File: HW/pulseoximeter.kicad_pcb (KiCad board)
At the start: 4 copper layers, 42.5 x 82.4 mm, 49 parts, among them J1 X05A20L15T, J2 TYPE-C-31-M-12, U1 TPD2EUSB30DRTR, U2 TPS7A4700RGWR, U3 ESP32-S3-MINI-1-N8, U4 LM324, U6 OPA140AIDBVR

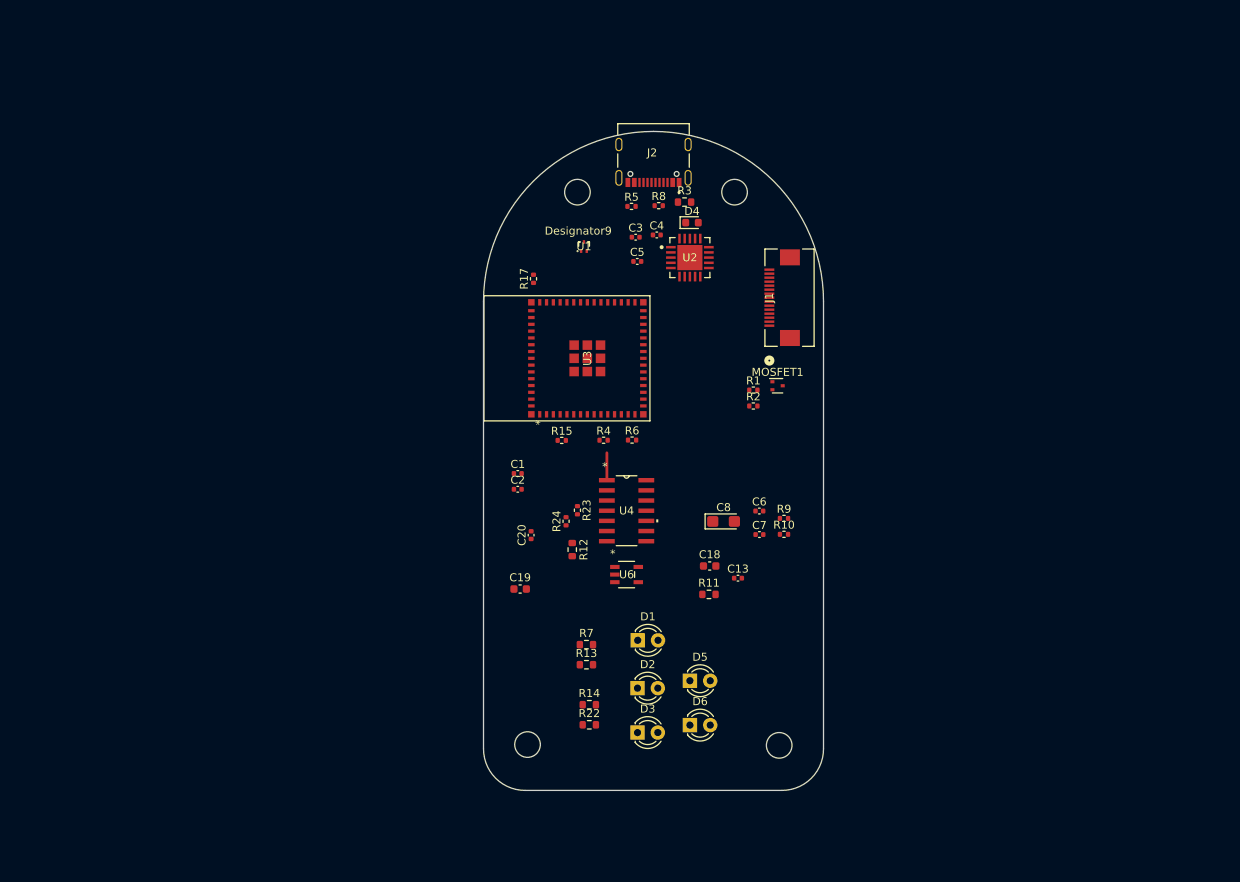
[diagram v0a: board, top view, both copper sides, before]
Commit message: implemented dynamic chart y-axis scaling
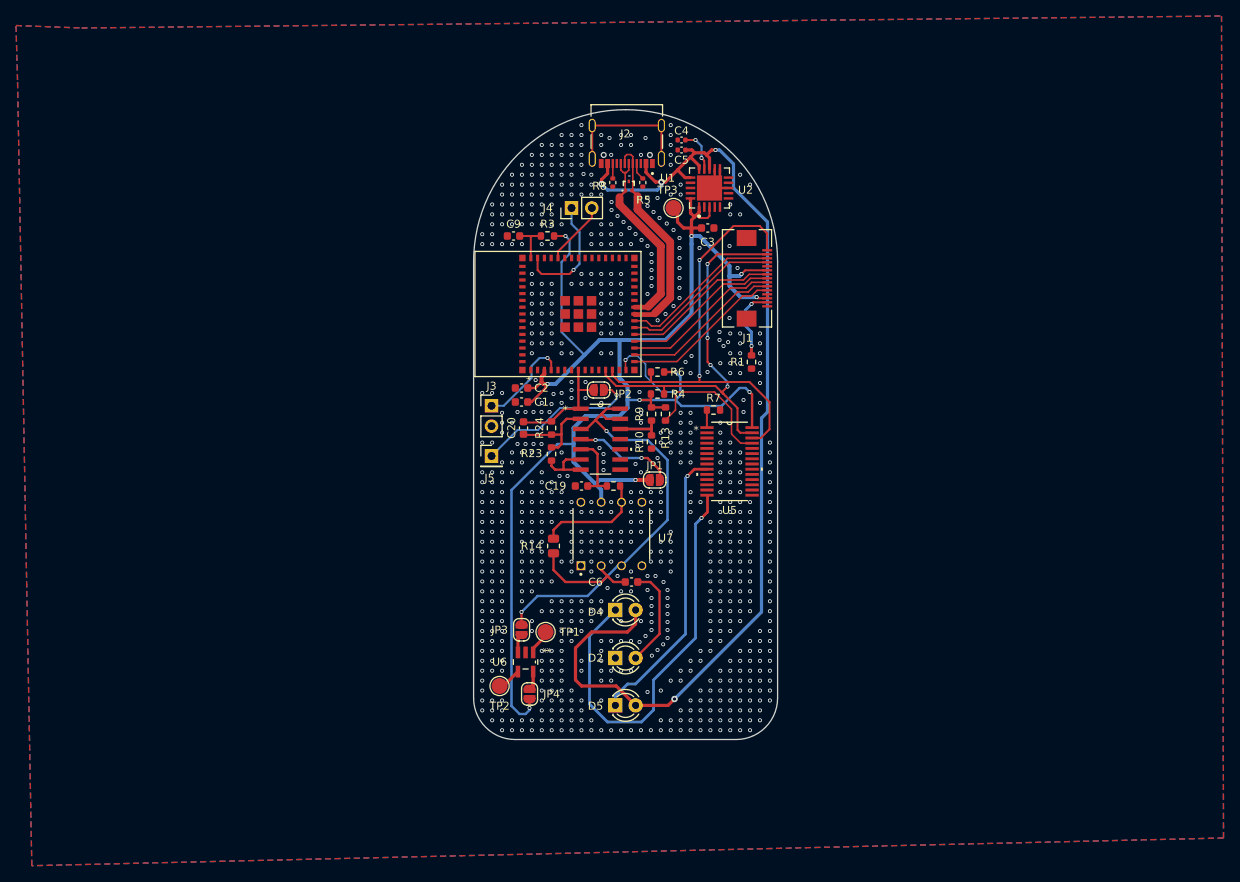
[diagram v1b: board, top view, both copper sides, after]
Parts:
- removed C13, C7: 0.1uF, Capacitor_SMD:C_0402_1005Metric
- removed C18: 440pF, Capacitor_SMD:C_0603_1608Metric
- removed C8: 1uF, Capacitor_Tantalum_SMD:CP_EIA-3216-10_Kemet-I
- removed D1: D_Photo, LED_THT:LED_D3.0mm
- removed D3, D6: LED, LED_THT:LED_D3.0mm
- removed MOSFET1: DMN2310UT-13, Package_TO_SOT_SMD:SOT-523
- removed R11: 8.1M, Resistor_SMD:R_0603_1608Metric
- removed R15, R17: 10k, Resistor_SMD:R_0402_1005Metric
- removed R2: 1M, Resistor_SMD:R_0402_1005Metric
- removed R22: 330, Resistor_SMD:R_0603_1608Metric
- removed REF** (x4): MountingHole_3.2mm_M3, MountingHole:MountingHole_3.2mm_M3
- added C9: 0.1uF, Capacitor_SMD:C_0603_1608Metric, F.Cu at (131.5, 68.5)
- added J3: Conn_01x02, Connector_PinHeader_2.54mm:PinHeader_1x02_P2.54mm_Vertical, F.Cu at (128.8, 89.7)
- added J4: Conn_01x02, Connector_PinHeader_2.54mm:PinHeader_1x02_P2.54mm_Vertical, F.Cu at (138.8, 65.0)
- added J5: Conn_01x01_Socket, Connector_PinHeader_2.54mm:PinHeader_1x01_P2.54mm_Vertical, F.Cu at (128.8, 96.0)
- added JP1: SolderJumper_2_Open, Jumper:SolderJumper-2_P1.3mm_Open_RoundedPad1.0x1.5mm, F.Cu at (149.2, 99.0)
- added JP2: SolderJumper_2_Open, Jumper:SolderJumper-2_P1.3mm_Open_RoundedPad1.0x1.5mm, F.Cu at (142.2, 87.8)
- added JP3: SolderJumper_2_Open, Jumper:SolderJumper-2_P1.3mm_Open_RoundedPad1.0x1.5mm, F.Cu at (132.5, 117.7)
- added JP4: SolderJumper_2_Open, Jumper:SolderJumper-2_P1.3mm_Open_RoundedPad1.0x1.5mm, F.Cu at (133.5, 125.8)
- added TP1: TestPoint, TestPoint:TestPoint_Pad_D2.0mm, F.Cu at (135.5, 118.0)
- added TP2: TestPoint, TestPoint:TestPoint_Pad_D2.0mm, F.Cu at (129.8, 124.8)
- added TP3: TestPoint, TestPoint:TestPoint_Pad_D2.0mm, F.Cu at (151.5, 65.0)
- added U5: TLC59116IPWR, TLC59116IPWR:PW28, F.Cu at (158.5, 96.7)
- added U7: LMC6001BIN/NOPB, LMC6001BIN_NOPB:DIP794W45P254L959H508Q8, F.Cu at (143.7, 105.8)
- C1, C2, C20, C3: footprint Capacitor_SMD:C_0402_1005Metric -> Capacitor_SMD:C_0603_1608Metric
- C6: value 10uF -> 0.22uF; footprint Capacitor_SMD:C_0402_1005Metric -> Capacitor_SMD:C_0603_1608Metric
- D2: value LED -> D_Photo
- D4: footprint LED_SMD:LED_0603_1608Metric -> LED_THT:LED_D3.0mm
- R1: value 10k -> 0; footprint Resistor_SMD:R_0402_1005Metric -> Resistor_SMD:R_0603_1608Metric
- R10, R23, R24, R4, R6, R9: footprint Resistor_SMD:R_0402_1005Metric -> Resistor_SMD:R_0603_1608Metric
- R12: value 33k -> 22k
- R13: value 330 -> 10k
- R14: value 330 -> 5.6M; footprint Resistor_SMD:R_0603_1608Metric -> Resistor_SMD:R_0805_2012Metric
- R3: value 1k -> 10k
- R7: value 330 -> 910
- U6: footprint OPA140AIDBVR:DBV5-M -> OPA140AIDBVR:DBV5
- moved D4 49.4 mm to (144.2, 115.2)
- moved R7 33.4 mm to (156.5, 90.2), turned to 180 degrees
- moved R13 32.9 mm to (150.5, 90.8), turned to 90 degrees
- moved R9 21.1 mm to (148.8, 90.8), turned to -90 degrees
- moved R14 20.3 mm to (136.5, 107.2), turned to -90 degrees
- moved R10 20.2 mm to (148.8, 94.2), turned to -90 degrees
- moved C6 18.3 mm to (146.2, 111.8), turned to 180 degrees
- moved R3 17.6 mm to (135.8, 68.5), turned to 180 degrees
- moved U6 16.7 mm to (133.0, 121.8), turned to -90 degrees
- moved C19 15.0 mm to (140.0, 99.8), turned to 180 degrees
- moved C5 15.0 mm to (152.5, 57.8), turned to 180 degrees
- moved C20 13.4 mm to (132.8, 92.5), turned to -90 degrees
- moved C2 12.7 mm to (132.5, 87.5), turned to 180 degrees
- moved C4 12.3 mm to (152.5, 56.5)
- moved R24 11.8 mm to (136.3, 92.5), turned to -90 degrees
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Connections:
- C20 pad 2: Net-(U4A-+) -> Net-(U4A--)
- C6 pad 1: VBUS -> Net-(D2-A)
- C6 pad 2: GND -> Net-(U7-IN-)
- D4 pad 1: GND -> Net-(D4-K)
- D4 pad 2: Net-(D4-A) -> VBUS
- D5 pad 1: GND -> Net-(D5-K)
- D5 pad 2: Net-(D5-A) -> VBUS
- J1 pad 1: GND -> SCL
- J1 pad 10: +3.3V -> /DISPLAY_CS
- J1 pad 11: GND -> /DISPLAY_D/C
- J1 pad 12: /TP_RST -> +3.3V
- J1 pad 13: /TP_INT -> +3.3V
- J1 pad 14: SDA -> Net-(J1-Pad14)
- J1 pad 15: SCL -> GND
- J1 pad 2: /LEDK -> SDA
- J1 pad 3: +3.3V -> /TP_INT
- J1 pad 4: +3.3V -> /TP_RST
- J1 pad 5: /DISPLAY_D/C -> GND
- J1 pad 6: /DISPLAY_CS -> +3.3V
- J1 pad 7: /DISPLAY_CLK -> /DISPLAY_RESET
- J1 pad 9: /DISPLAY_RESET -> /DISPLAY_CLK
- R1 pad 1: Net-(MOSFET1-G) -> GND
- R1 pad 2: /BACKLIGHT_EN -> Net-(J1-Pad14)
- R10 pad 1: Net-(U4D--) -> Net-(U4D-+)
- R12 pad 2: Net-(U6-OUT) -> Net-(U7-OUT)
- R13 pad 1: VBUS -> /LED_RST
- R13 pad 2: Net-(D6-A) -> +3.3V
- R14 pad 1: VBUS -> Net-(U7-OUT)
- R14 pad 2: Net-(D2-A) -> Net-(U7-IN-)
- R23 pad 1: Net-(U4A-+) -> Net-(U4A--)
- R24 pad 2: Net-(U4A-+) -> Net-(U4A--)
- R3 pad 1: VBUS -> +3.3V
- R3 pad 2: Net-(D4-A) -> Net-(U3-EN)
- R7 pad 1: VBUS -> GND
- R7 pad 2: Net-(D5-A) -> Net-(U5-REXT)
- R9 pad 2: Net-(U4D--) -> Net-(U4D-+)
- U1 pad 1: DN -> DP
- U3 pad 14: /DISPLAY_CS -> unconnected-(U3-IO10-Pad14)
- U3 pad 15: /DISPLAY_SDI -> /LED_RST
- U3 pad 16: /DISPLAY_CLK -> /DISPLAY_D/C
- U3 pad 17: /DISPLAY_D/C -> /DISPLAY_CS
- U3 pad 18: /DISPLAY_RESET -> /DISPLAY_CLK
- U3 pad 19: /TP_RST -> /DISPLAY_SDI
- U3 pad 20: /TP_INT -> /DISPLAY_RESET
- U3 pad 21: unconnected-(U3-IO17-Pad21) -> /TP_RST
- U3 pad 22: unconnected-(U3-IO18-Pad22) -> /TP_INT
- U3 pad 27: /BACKLIGHT_EN -> unconnected-(U3-IO47-Pad27)
- U3 pad 39: ESP32_RX -> unconnected-(U3-TXD0-Pad39)
- U3 pad 4: Net-(U3-IO0) -> /IO0
- U3 pad 40: ESP32_TX -> unconnected-(U3-RXD0-Pad40)
- U3 pad 41: unconnected-(U3-IO45-Pad41) -> /VDD_SPI_V
- U3 pad 44: unconnected-(U3-IO46-Pad44) -> /ROM_MSG
- U4 pad 12: VCC/2 -> Net-(U4D-+)
- U4 pad 13: Net-(U4D--) -> VCC/2
- U4 pad 2: VCC/2 -> Net-(U4A--)
- U4 pad 3: Net-(U4A-+) -> VCC/2
- U4 pad 4: VBUS -> Net-(JP1-B)
- U6 pad 3: VCC/2 -> Net-(JP3-B)
- U6 pad 5: VBUS -> Net-(JP4-B)
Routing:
- net +3.3V: track 0.00 -> 199.3 mm, vias 0 -> 10
- net VBUS: track 0.00 -> 135.7 mm, vias 0 -> 4
- net SCL: track 0.00 -> 56.9 mm, vias 0 -> 2
- net Net-(D4-K): track 0.00 -> 52.3 mm, vias 0 -> 1
- net VCC/2: track 0.00 -> 51.7 mm, vias 0 -> 2
- net SDA: track 0.00 -> 50.3 mm, vias 0 -> 4
- net Net-(D5-K): track 0.00 -> 35.8 mm, vias 0 -> 1
- net /LED_RST: track 0.00 -> 28.6 mm, vias 0 -> 2
- net DN: track 0.00 -> 27.2 mm
- net DP: track 0.00 -> 24.6 mm
- net Net-(J5-Pin_1): track 0.00 -> 20.9 mm, vias 0 -> 1
- net /DISPLAY_D/C: track 0.00 -> 20.3 mm
- net /DISPLAY_CS: track 0.00 -> 20.1 mm
- net /DISPLAY_CLK: track 0.00 -> 20.0 mm
- net /TP_INT: track 0.00 -> 19.9 mm
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- added copper zone on B.Cu, net GND
- added copper zone on F.Cu, net GND
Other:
- board size 42.5 x 82.4 mm -> 38 x 78.7 mm
- copper layers 4 -> 2
